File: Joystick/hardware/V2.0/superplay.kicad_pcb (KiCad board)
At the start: 4 copper layers, 36 parts, among them J1 AVR-PDI-6A, J2 CONN_02X04, J3 USB_B, U1 MCP1700T-3002E, U2 ATXMEGA128A3U-A, U3 TPD4S009DBV, Y1 16MHz

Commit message: Layer numbers
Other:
- board text added: "2"
- board text added: "3"
- board text added: "4"
- board text added: "© 2017 Paul Qureshi"
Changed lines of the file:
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@@
     (area 0 0 0 0)
     (thickness 1.6)
-    (drawings 224)
+    (drawings 229)
     (tracks 596)
     (zones 0)
@@
   (page A4)
   (layers
-    (0 F.Cu signal hide)
-    (1 PWR signal hide)
-    (2 GND signal hide)
+    (0 F.Cu signal)
+    (1 PWR signal)
+    (2 GND signal)
     (31 B.Cu signal)
     (32 B.Adhes user)
@@
     (pad_to_mask_clearance 0.2)
     (aux_axis_origin 0 0)
-    (visible_elements 7FFEBF9F)
+    (visible_elements 7FFEFF9F)
     (pcbplotparams
       (layerselection 0x00030_80000001)
@@
       (rotate (xyz 0 0 90))
     )
+  )
+  (gr_text 4 (at 50.9 64.1) (layer B.Cu)
+    (effects (font (size 1.5 1.5) (thickness 0.3)))
+  )
+  (gr_text 3 (at 51 62) (layer GND)
+    (effects (font (size 1.5 1.5) (thickness 0.3)))
+  )
+  (gr_text 2 (at 51 60) (layer PWR)
+    (effects (font (size 1.5 1.5) (thickness 0.3)))
+  )
+  (gr_text 1 (at 51 58) (layer F.Cu)
+    (effects (font (size 1.5 1.5) (thickness 0.3)))
+  )
+  (gr_text "© 2017\nPaul Qureshi" (at 77.6 79.6 90) (layer B.Cu)
+    (effects (font (size 1 1) (thickness 0.15)) (justify left mirror))
   )
   (gr_text J2 (at 71.3 98 90) (layer Eco1.User)
@@
     (polygon
       (pts
-        (xy 50 50) (xy 80 50) (xy 80 100) (xy 50 100)
+        (xy 50 50) (xy 80 50) (xy 80 100) (xy 50 100) (xy 50 65.1)
+        (xy 51.7 65.1) (xy 51.7 56.9) (xy 50 56.9)
       )
     )
@@
     (polygon
       (pts
-        (xy 50 50) (xy 80 50) (xy 80 100) (xy 50 100)
+        (xy 50 50) (xy 80 50) (xy 80 100) (xy 50 100) (xy 50 65.1)
+        (xy 51.7 65.1) (xy 51.7 56.9) (xy 50 56.9)
       )
     )

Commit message: Added SUPERPLAY logo
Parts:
- added G***: LOGO, Keio:superplay1.1_two_line_10.7x5.0, B.Cu at (65.5, 60.0)
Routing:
- net /LED: track 12.4 -> 16.1 mm
- net GND: track 87.1 -> 85.6 mm
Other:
- board text added: "D1"
- board text added: "J3"

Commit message: Keio + graphic
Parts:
- added G***: LOGO, Keio:logo2_7.5x2.3mm, B.Cu at (55.5, 60.0)

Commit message: KEIO logo was backwards
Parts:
- turned G*** to 180 degrees
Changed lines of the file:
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@@
     (links 0)
     (no_connects 0)
-    (area 27 42.3 92.85 101.505733)
+    (area 49.899999 42.3 92.85 101.505733)
     (thickness 1.6)
     (drawings 232)
@@
     (visible_elements 7FFEBF9F)
     (pcbplotparams
-      (layerselection 0x00030_80000001)
-      (usegerberextensions false)
+      (layerselection 0x02cc0_80000007)
+      (usegerberextensions true)
       (excludeedgelayer true)
       (linewidth 0.100000)
@@
       (plotinvisibletext false)
       (padsonsilk false)
-      (subtractmaskfromsilk false)
+      (subtractmaskfromsilk true)
       (outputformat 1)
       (mirror false)
-      (drillshape 1)
+      (drillshape 0)
       (scaleselection 1)
-      (outputdirectory ""))
+      (outputdirectory plot/))
   )
   (net 0 "")
@@
   )
   (module Keio:logo2_7.5x2.3mm (layer B.Cu)
-    (at 55.5 60)
-    (fp_text reference G*** (at 0 0) (layer B.SilkS) hide
+    (at 55.5 60 180)
+    (fp_text reference G*** (at 0 0 180) (layer B.SilkS) hide
       (effects (font (thickness 0.3)) (justify mirror))
     )
-    (fp_text value LOGO (at 0.75 0) (layer B.SilkS) hide
+    (fp_text value LOGO (at 0.75 0 180) (layer B.SilkS) hide
       (effects (font (thickness 0.3)) (justify mirror))
     )

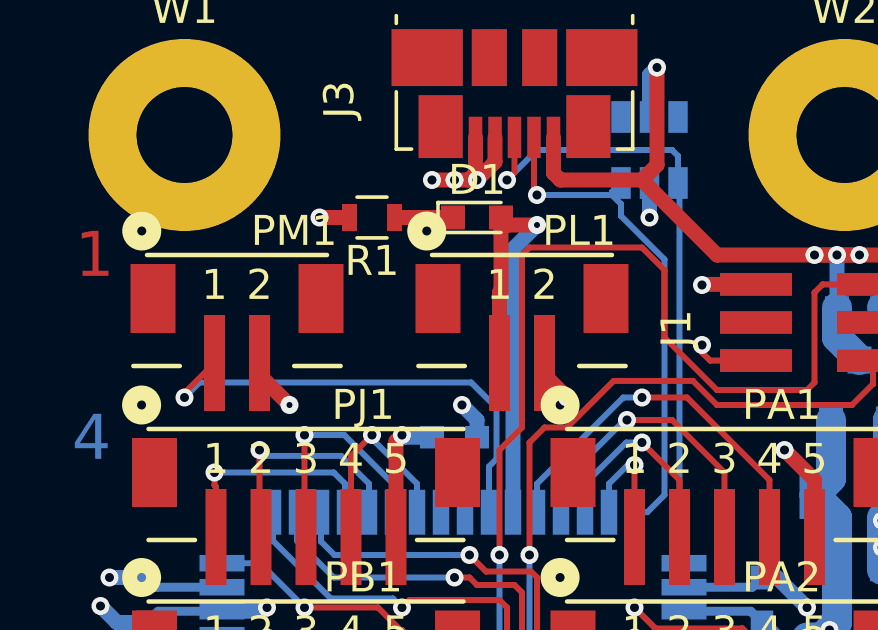
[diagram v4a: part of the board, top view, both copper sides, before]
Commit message: Min hole size fixed, drill file for Seeed OK
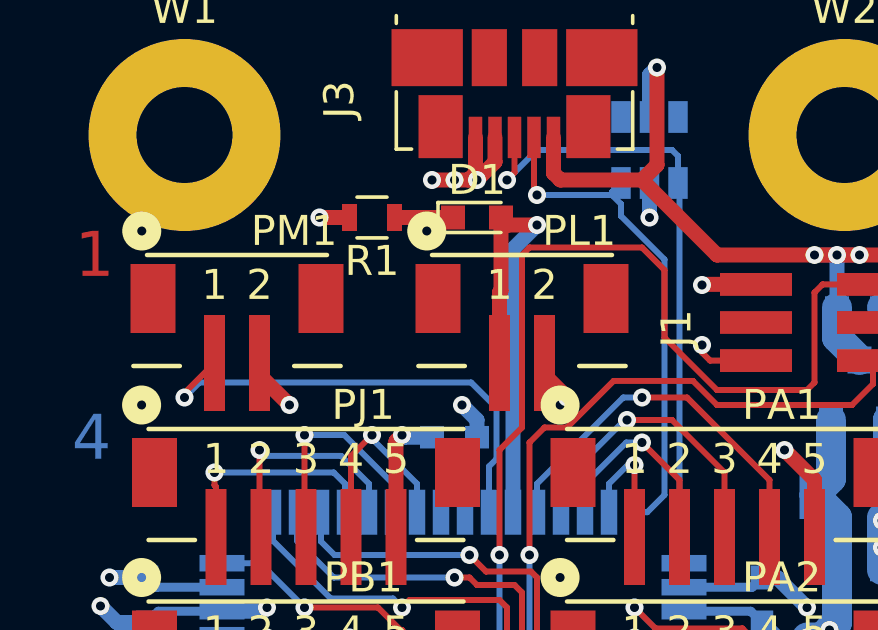
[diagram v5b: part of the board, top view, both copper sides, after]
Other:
- board text added: "Top silkscreen: Eco1.User Bottom silkscreen; Eco2.User Min hole: 0.3mm Min tracking/spacing: 6mil"
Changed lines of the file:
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@@
 (kicad_pcb (version 4) (host pcbnew 4.0.5)
   (general
-    (links 0)
+    (links 118)
     (no_connects 0)
     (area 49.899999 42.3 92.85 101.505733)
     (thickness 1.6)
-    (drawings 232)
+    (drawings 233)
     (tracks 601)
     (zones 0)
@@
     (visible_elements 7FFEBF9F)
     (pcbplotparams
-      (layerselection 0x02cc0_80000007)
+      (layerselection 0x020c0_80000007)
       (usegerberextensions true)
       (excludeedgelayer true)
@@
       (xy 1.910817 1.127456) (xy 2.837161 1.127979) (xy 3.763506 1.128501) (xy 3.762971 0.203125)) (layer Eco2.User) (width 0.01))
   )
+  (gr_text "Top silkscreen: Eco1.User\nBottom silkscreen; Eco2.User\n\nMin hole: 0.3mm\nMin tracking/spacing: 6mil" (at 90 57.5) (layer Cmts.User)
+    (effects (font (size 1.5 1.5) (thickness 0.3)) (justify left))
+  )
   (gr_text J3 (at 71 54.25 90) (layer Eco1.User)
     (effects (font (size 1.5 1.5) (thickness 0.3)))
@@
   (segment (start 66 61.6) (end 66 62) (width 0.5) (layer F.Cu) (net 2))
   (segment (start 66 62) (end 66.75 62.75) (width 0.5) (layer F.Cu) (net 2))
-  (via (at 66.75 62.75) (size 0.6) (drill 0.2) (layers F.Cu B.Cu) (net 2))
+  (via (at 66.75 62.75) (size 0.6) (drill 0.3) (layers F.Cu B.Cu) (net 2))
   (segment (start 56.5 61.6) (end 56.5 62) (width 0.5) (layer F.Cu) (net 2))
   (segment (start 56.5 62) (end 57.5 63) (width 0.5) (layer F.Cu) (net 2))
-  (via (at 57.5 63) (size 0.6) (drill 0.2) (layers F.Cu B.Cu) (net 2))
+  (via (at 57.5 63) (size 0.6) (drill 0.3) (layers F.Cu B.Cu) (net 2))
   (segment (start 52.75 70.25) (end 51.75 70.25) (width 0.5) (layer B.Cu) (net 2))
   (segment (start 51.75 70.25) (end 51.2 69.7) (width 0.5) (layer B.Cu) (net 2))
@@
   (segment (start 64.8 57) (end 64.55 56.75) (width 0.5) (layer F.Cu) (net 6))
   (segment (start 64.95 59.7) (end 64.95 57.8) (width 0.5) (layer B.Cu) (net 6))
-  (via (at 65.75 57) (size 0.6) (drill 0.2) (layers F.Cu B.Cu) (net 6))
+  (via (at 65.75 57) (size 0.6) (drill 0.3) (layers F.Cu B.Cu) (net 6))
   (segment (start 64.95 57.8) (end 65.75 57) (width 0.5) (layer B.Cu) (net 6))
   (segment (start 64.55 56.75) (end 64.55 59.2) (width 0.5) (layer F.Cu) (net 6))
